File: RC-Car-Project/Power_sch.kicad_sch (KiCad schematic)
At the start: 0 parts

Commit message: Power: add converters
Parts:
- added C1, C2: 10u/50V, symbol Device:C
- added U2: XL1509-5.0, Package_SO:SOIC-8_3.9x4.9mm_P1.27mm, symbol Regulator_Switching:XL1509-5.0
- added U3: LT1963AxST-3.3, Package_TO_SOT_SMD:SOT-223-3_TabPin2, symbol Regulator_Linear:LT1963AxST-3.3
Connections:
- new net: C1.1, U3.1 (IN)
- new net: U2.5 (GND), U2.6 (GND), U2.7 (GND), U2.8 (GND)
- new net +3V3: C2.1, U3.3 (OUT)
- new net GND_3V3: C2.2, U3.2 (GND)
- new net GND_BATT: C1.2
- new net VDD_BATT: U2.1 (VIN)

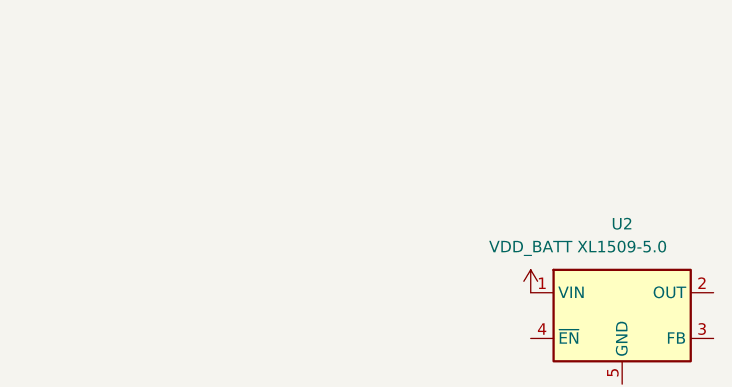
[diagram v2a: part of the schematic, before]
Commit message: Add libraries and components in schs
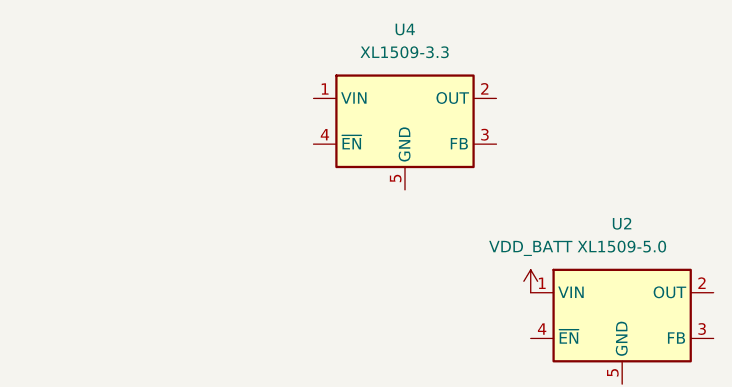
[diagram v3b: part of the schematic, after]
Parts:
- added U4: XL1509-3.3, Package_SO:SOIC-8_3.9x4.9mm_P1.27mm, symbol Regulator_Switching:XL1509-3.3
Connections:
- new net: U4.5 (GND), U4.6 (GND), U4.7 (GND), U4.8 (GND)
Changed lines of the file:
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@@
+	)
+	(symbol
+		(lib_id "Regulator_Switching:XL1509-3.3")
+		(at 143.51 48.26 0)
+		(unit 1)
+		(exclude_from_sim no)
+		(in_bom yes)
+		(on_board yes)
+		(dnp no)
+		(fields_autoplaced yes)
+		(property "Reference" "U4"
+			(at 143.51 38.1 0)
+			(effects
+				(font
+					(size 1.27 1.27)
+				)
+			)
+		)
+		(property "Value" "XL1509-3.3"
+			(at 143.51 40.64 0)
+			(effects
+				(font
+					(size 1.27 1.27)
+				)
+			)
+		)
+		(property "Footprint" "Package_SO:SOIC-8_3.9x4.9mm_P1.27mm"
+			(at 143.51 39.878 0)
+			(effects
+				(font
+					(size 1.27 1.27)
+				)
+				(hide yes)
+			)
+		)
+		(property "Datasheet" "https://datasheet.lcsc.com/lcsc/1809050422_XLSEMI-XL1509-5-0E1_C61063.pdf"
+			(at 146.05 37.592 0)
+			(effects
+				(font
+					(size 1.27 1.27)
+				)
+				(hide yes)
+			)
+		)
+		(property "Description" "Buck DC/DC Converter, 2A, 3.3V Output Voltage, 4.5-40V Input Voltage"
+			(at 143.51 48.26 0)
+			(effects
+				(font
+					(size 1.27 1.27)
+				)
+				(hide yes)
+			)
+		)
+		(pin "3"
+		)
+		(pin "2"
+		)
+		(pin "6"
+		)
+		(pin "7"
+		)
+		(pin "8"
+		)
+		(pin "5"
+		)
+		(pin "1"
+		)
+		(pin "4"
+		)
+		(instances
+			(project ""
+				(path "/ba870fd1-751d-4755-8e1a-1ea86ca9e2f6/e8cbdd69-5fc8-4583-a262-8a3c06e86dab"
+					(reference "U4")
+					(unit 1)
+				)
+			)
+		)
 	)
 	(symbol

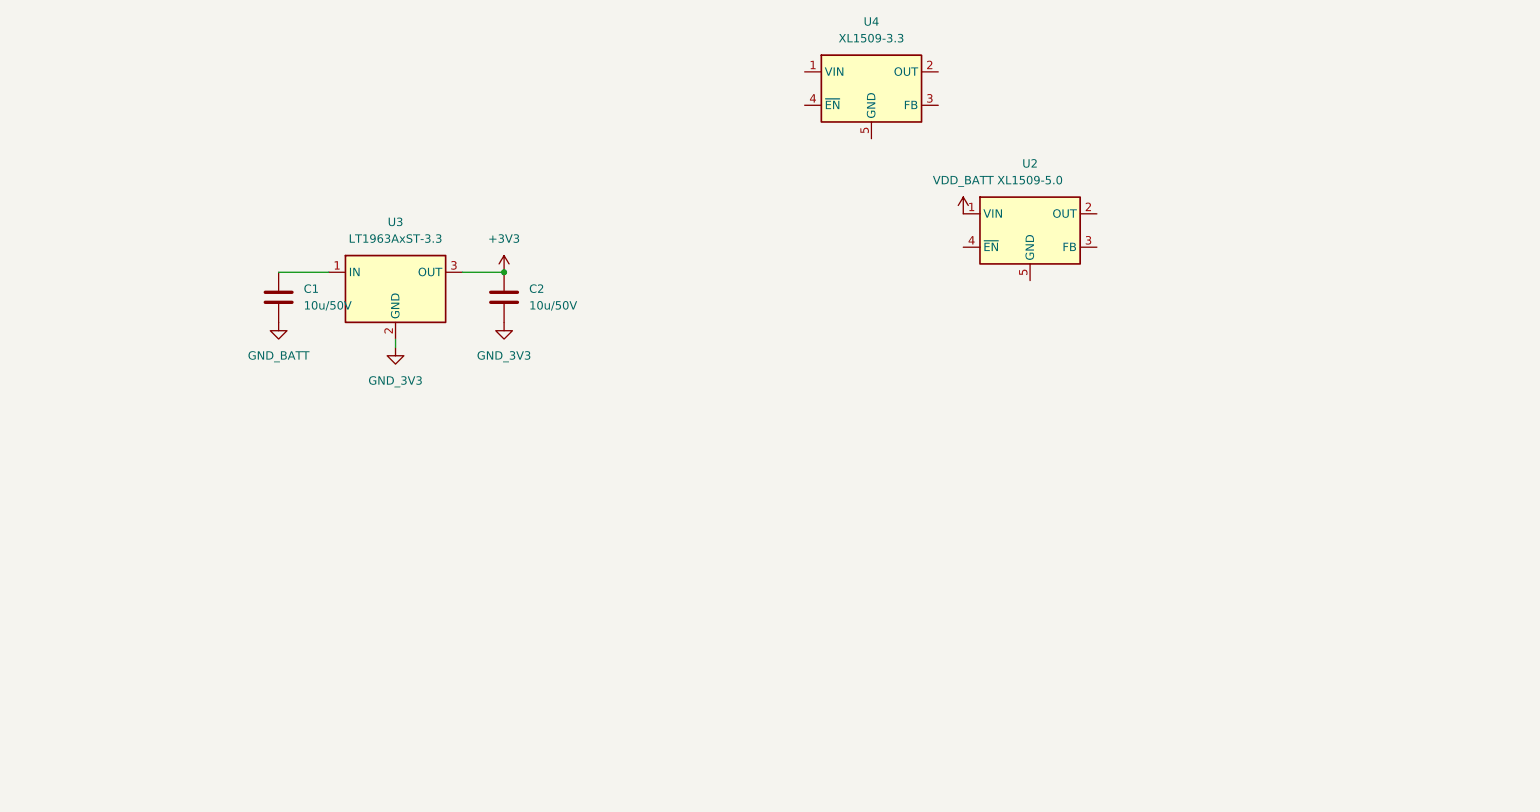
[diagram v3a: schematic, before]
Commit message: Added Basic Schematic + STM32 Project config. TODO: Component value selection + double check all connections.
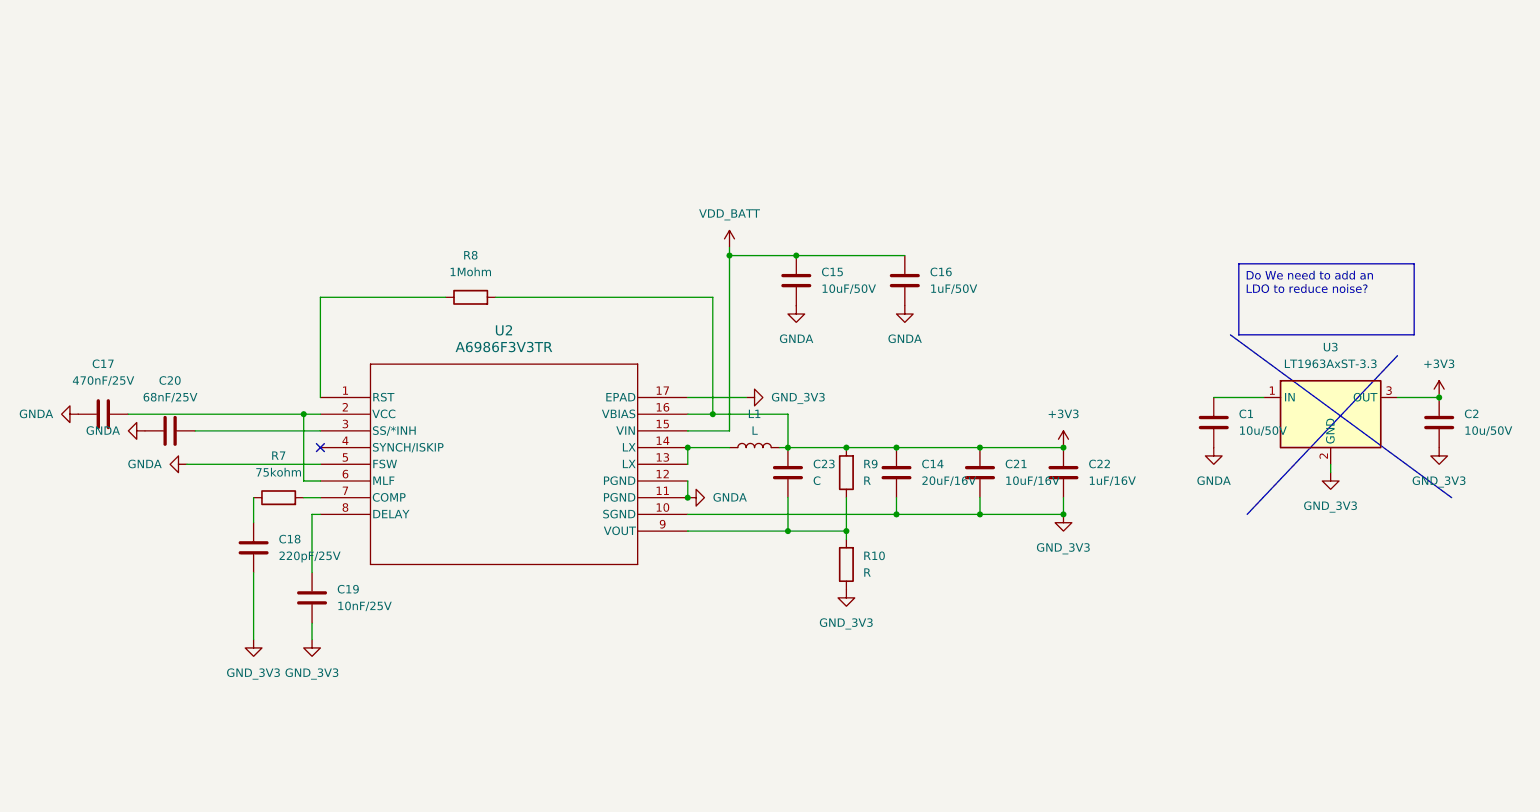
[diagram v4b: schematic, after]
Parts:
- removed U2: XL1509-5.0, Package_SO:SOIC-8_3.9x4.9mm_P1.27mm, symbol Regulator_Switching:XL1509-5.0
- removed U4: XL1509-3.3, Package_SO:SOIC-8_3.9x4.9mm_P1.27mm, symbol Regulator_Switching:XL1509-3.3
- added C14: 20uF/16V, symbol Device:C
- added C15: 10uF/50V, symbol Device:C
- added C16: 1uF/50V, symbol Device:C
- added C17: 470nF/25V, symbol Device:C
- added C18: 220pF/25V, symbol Device:C
- added C19: 10nF/25V, symbol Device:C
- added C20: 68nF/25V, symbol Device:C
- added C21: 10uF/16V, symbol Device:C
- added C22: 1uF/16V, symbol Device:C
- added C23: C, symbol Device:C
- added L1: L, symbol Device:L
- added R10, R9: R, symbol Device:R
- added R7: 75kohm, symbol Device:R
- added R8: 1Mohm, symbol Device:R
- added U2: A6986F3V3TR, HTSSOP16_4P5X5P1X0P65P_STM, symbol A6986F3V3TR:A6986F3V3TR
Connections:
- net +3V3: now also C14.1, C21.1, C22.1, C23.1, L1.2, R8.2, R9.2, U2.16 (VBIAS)
- net GND_3V3: now also C14.2, C18.1, C19.2, C21.2, C22.2, R10.1, U2.10 (SGND), U2.17 (EPAD)
- net VDD_BATT: now also C15.1, C16.1, U2.15 (VIN)
- net GND_BATT renamed GNDA
- net GNDA: now also C15.2, C16.2, C17.2, C20.2, U2.11 (PGND), U2.12 (PGND), U2.5 (FSW)
- new net: R8.1, U2.1 (RST)
- new net: L1.1, U2.13 (LX), U2.14 (LX)
- new net: C17.1, U2.2 (VCC), U2.6 (MLF)
- new net: C20.1, U2.3 (SS/*INH)
- new net: R7.2, U2.7 (COMP)
- new net: C19.1, U2.8 (DELAY)
- new net: C23.2, R10.2, R9.1, U2.9 (VOUT)
- new net: C18.2, R7.1
- no-connect marks 0 -> 1
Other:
- moved on the sheet: C1, C2, U3

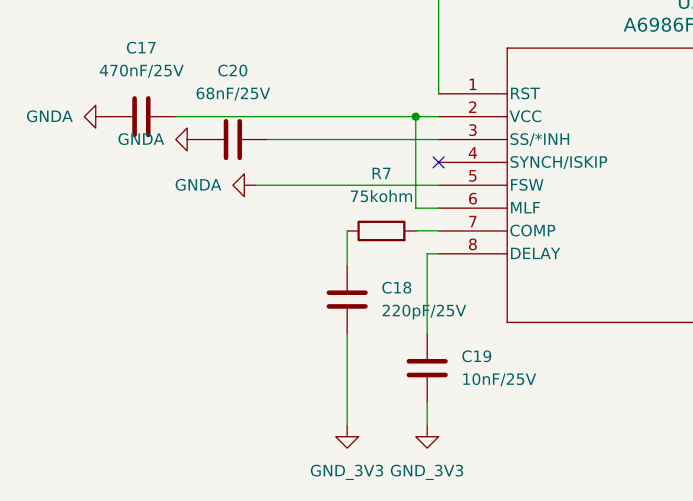
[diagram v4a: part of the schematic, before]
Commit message: Added footprints + final parts. (Need to finish buck converter next)
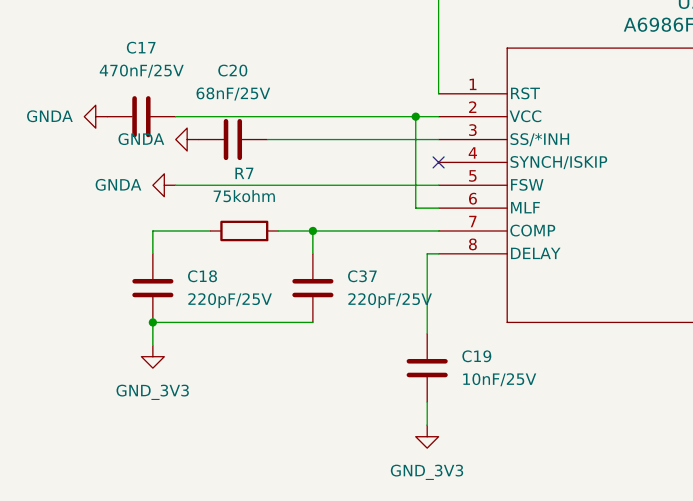
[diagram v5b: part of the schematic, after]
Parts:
- added C37: 220pF/25V, Capacitor_SMD:C_0201_0603Metric, symbol Device:C
- C16, C17, C18, C19, C20, C22, C23: footprint (none) -> Capacitor_SMD:C_0201_0603Metric
- L1: footprint (none) -> Inductor_SMD_Wurth:L_Wurth_WE-LQSH-4020
- R10, R7, R8, R9: footprint (none) -> Resistor_SMD:R_0201_0603Metric
- U2: footprint HTSSOP16_4P5X5P1X0P65P_STM -> footprints:HTSSOP16_4P5X5P1X0P65P_STM
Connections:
- net GND_3V3: now also C37.1
- net at R7.2, U2.7 (COMP): now also C37.2
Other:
- moved on the sheet: C18, R7
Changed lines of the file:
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@@
 	)
 	(junction
+		(at 27.94 120.65)
+		(diameter 0)
+		(color 0 0 0 0)
+	)
+	(junction
+		(at 45.72 110.49)
+		(diameter 0)
+		(color 0 0 0 0)
+	)
+	(junction
 		(at 130.81 115.57)
 		(diameter 0)
@@
 	(wire
 		(pts
+			(xy 45.72 113.03) (xy 45.72 110.49)
+		)
+		(stroke
+			(width 0)
+			(type default)
+		)
+	)
+	(wire
+		(pts
 			(xy 59.69 107.95) (xy 57.15 107.95)
 		)
@@
 	(wire
 		(pts
-			(xy 57.15 110.49) (xy 59.69 110.49)
+			(xy 41.91 110.49) (xy 45.72 110.49)
 		)
 		(stroke
@@
 	(wire
 		(pts
+			(xy 27.94 110.49) (xy 34.29 110.49)
+		)
+		(stroke
+			(width 0)
+			(type default)
+		)
+	)
+	(wire
+		(pts
 			(xy 57.15 97.79) (xy 59.69 97.79)
 		)
@@
 	(wire
 		(pts
+			(xy 27.94 120.65) (xy 45.72 120.65)
+		)
+		(stroke
+			(width 0)
+			(type default)
+		)
+	)
+	(wire
+		(pts
 			(xy 58.42 113.03) (xy 59.69 113.03)
 		)
@@
 	(wire
 		(pts
+			(xy 45.72 110.49) (xy 59.69 110.49)
+		)
+		(stroke
+			(width 0)
+			(type default)
+		)
+	)
+	(wire
+		(pts
 			(xy 130.81 102.87) (xy 139.7 102.87)
 		)
@@
 	(wire
 		(pts
-			(xy 59.69 80.01) (xy 78.74 80.01)
+			(xy 27.94 110.49) (xy 27.94 113.03)
 		)
 		(stroke
@@
 	(wire
 		(pts
-			(xy 115.57 102.87) (xy 121.92 102.87)
+			(xy 59.69 80.01) (xy 78.74 80.01)
 		)
 		(stroke
@@
 	(wire
 		(pts
-			(xy 121.92 73.66) (xy 121.92 100.33)
+			(xy 115.57 102.87) (xy 121.92 102.87)
 		)
 		(stroke
@@
 	(wire
 		(pts
-			(xy 119.38 80.01) (xy 119.38 97.79)
+			(xy 121.92 73.66) (xy 121.92 100.33)
 		)
 		(stroke
@@
 	(wire
 		(pts
-			(xy 130.81 102.87) (xy 130.81 97.79)
+			(xy 119.38 80.01) (xy 119.38 97.79)
 		)
 		(stroke
@@
 	(wire
 		(pts
-			(xy 58.42 121.92) (xy 58.42 113.03)
+			(xy 130.81 102.87) (xy 130.81 97.79)
 		)
 		(stroke
@@
 	(wire
 		(pts
-			(xy 49.53 110.49) (xy 49.53 114.3)
+			(xy 58.42 121.92) (xy 58.42 113.03)
 		)
 		(stroke
@@
 	(wire
 		(pts
-			(xy 39.37 105.41) (xy 59.69 105.41)
+			(xy 30.48 105.41) (xy 59.69 105.41)
 		)
 		(stroke
@@
 	(wire
 		(pts
-			(xy 49.53 132.08) (xy 49.53 121.92)
+			(xy 27.94 123.19) (xy 27.94 120.65)
 		)
 		(stroke
@@
 	(symbol
 		(lib_id "power:GND")
-		(at 49.53 132.08 0)
+		(at 27.94 123.19 0)
 		(unit 1)
 		(exclude_from_sim no)
@@
 		(fields_autoplaced yes)
 		(property "Reference" "#PWR045"
-			(at 49.53 138.43 0)
+			(at 27.94 129.54 0)
 			(effects
 				(font
@@
 		)
 		(property "Value" "GND_3V3"
-			(at 49.53 137.16 0)
+			(at 27.94 128.27 0)
 			(effects
 				(font
@@
 		)
 		(property "Footprint" ""
-			(at 49.53 132.08 0)
+			(at 27.94 123.19 0)
 			(effects
 				(font
@@
 		)
 		(property "Datasheet" ""
-			(at 49.53 132.08 0)
+			(at 27.94 123.19 0)
 			(effects
 				(font
@@
 		)
 		(property "Description" "Power symbol creates a global label with name \"GND\" , ground"
-			(at 49.53 132.08 0)
+			(at 27.94 123.19 0)
 			(effects
 				(font
@@
 			)
 		)
-		(property "Footprint" "HTSSOP16_4P5X5P1X0P65P_STM"
+		(property "Footprint" "footprints:HTSSOP16_4P5X5P1X0P65P_STM"
 			(at 59.69 95.25 0)
 			(effects
@@
 			)
 		)
-		(property "Footprint" ""
+		(property "Footprint" "Capacitor_SMD:C_0201_0603Metric"
 			(at 22.86 98.7552 0)
 			(effects
@@
 			)
 		)
-		(property "Footprint" ""
+		(property "Footprint" "Inductor_SMD_Wurth:L_Wurth_WE-LQSH-4020"
 			(at 125.73 102.87 0)
 			(effects
@@
 	(symbol
 		(lib_id "Device:R")
-		(at 53.34 110.49 90)
+		(at 38.1 110.49 90)
 		(unit 1)
 		(exclude_from_sim no)
@@
 		(fields_autoplaced yes)
 		(property "Reference" "R7"
-			(at 53.34 104.14 90)
+			(at 38.1 104.14 90)
 			(effects
 				(font
@@
 		)
 		(property "Value" "75kohm"
-			(at 53.34 106.68 90)
+			(at 38.1 106.68 90)
 			(effects
 				(font
@@
 			)
 		)
-		(property "Footprint" ""
-			(at 53.34 112.268 90)
+		(property "Footprint" "Resistor_SMD:R_0201_0603Metric"
+			(at 38.1 112.268 90)
 			(effects
 				(font
@@
 		)
 		(property "Datasheet" "~"
-			(at 53.34 110.49 0)
+			(at 38.1 110.49 0)
 			(effects
 				(font
@@
 		)
 		(property "Description" "Resistor"
-			(at 53.34 110.49 0)
+			(at 38.1 110.49 0)
 			(effects
 				(font
@@
 			)
 		)
-		(property "Footprint" ""
+		(property "Footprint" "Capacitor_SMD:C_0201_0603Metric"
 			(at 33.02 101.2952 0)
 			(effects
@@
 			)
 		)
-		(property "Footprint" ""
+		(property "Footprint" "Capacitor_SMD:C_0201_0603Metric"
 			(at 173.6852 110.49 0)
 			(effects
@@
 			)
 		)
-		(property "Footprint" ""
+		(property "Footprint" "Resistor_SMD:R_0201_0603Metric"
 			(at 141.478 120.65 90)
 			(effects
@@
 			)
 		)
-		(property "Footprint" ""
+		(property "Footprint" "Resistor_SMD:R_0201_0603Metric"
 			(at 82.55 81.788 90)
 			(effects
@@
 			)
 		)
-		(property "Footprint" ""
+		(property "Footprint" "Capacitor_SMD:C_0201_0603Metric"
 			(at 149.5552 81.28 0)
 			(effects
@@
 	(symbol
 		(lib_id "Device:C")
+		(at 45.72 116.84 180)
+		(unit 1)
+		(exclude_from_sim no)
+		(in_bom yes)
+		(on_board yes)
+		(dnp no)
+		(fields_autoplaced yes)
+		(property "Reference" "C37"
+			(at 49.53 115.5699 0)
+			(effects
+				(font
+					(size 1.27 1.27)
+				)
+				(justify right)
+			)
+		)
+		(property "Value" "220pF/25V"
+			(at 49.53 118.1099 0)
+			(effects
+				(font
+					(size 1.27 1.27)
+				)
+				(justify right)
+			)
+		)
+		(property "Footprint" "Capacitor_SMD:C_0201_0603Metric"
+			(at 44.7548 113.03 0)
+			(effects
+				(font
+					(size 1.27 1.27)
+				)
+				(hide yes)
+			)
+		)
+		(property "Datasheet" "~"
+			(at 45.72 116.84 0)
+			(effects
+				(font
+					(size 1.27 1.27)
+				)
+				(hide yes)
+			)
+		)
+		(property "Description" "Unpolarized capacitor"
+			(at 45.72 116.84 0)
+			(effects
+				(font
+					(size 1.27 1.27)
+				)
+				(hide yes)
+			)
+		)
+		(pin "1"
+		)
+		(pin "2"
+		)
+		(instances
+			(project "RC-Car-Project"
+				(path "/ba870fd1-751d-4755-8e1a-1ea86ca9e2f6/e8cbdd69-5fc8-4583-a262-8a3c06e86dab"
+					(reference "C37")
+					(unit 1)
+				)
+			)
+		)
+	)
+	(symbol
+		(lib_id "Device:C")
 		(at 130.81 106.68 0)
 		(unit 1)
@@
 			)
 		)
-		(property "Footprint" ""
+		(property "Footprint" "Capacitor_SMD:C_0201_0603Metric"
 			(at 131.7752 110.49 0)
 			(effects
@@
 	(symbol
 		(lib_id "Device:C")
-		(at 49.53 118.11 180)
+		(at 27.94 116.84 180)
 		(unit 1)
 		(exclude_from_sim no)
@@
 		(fields_autoplaced yes)
 		(property "Reference" "C18"
-			(at 53.34 116.8399 0)
+			(at 31.75 115.5699 0)
 			(effects
 				(font
@@
 		)
 		(property "Value" "220pF/25V"
-			(at 53.34 119.3799 0)
+			(at 31.75 118.1099 0)
 			(effects
 				(font
@@
 			)
 		)
-		(property "Footprint" ""
-			(at 48.5648 114.3 0)
+		(property "Footprint" "Capacitor_SMD:C_0201_0603Metric"
+			(at 26.9748 113.03 0)
 			(effects
 				(font
@@
 		)
 		(property "Datasheet" "~"
-			(at 49.53 118.11 0)
+			(at 27.94 116.84 0)
 			(effects
 				(font
@@
 		)
 		(property "Description" "Unpolarized capacitor"
-			(at 49.53 118.11 0)
+			(at 27.94 116.84 0)
 			(effects
 				(font
@@
 			)
 		)
-		(property "Footprint" ""
+		(property "Footprint" "Resistor_SMD:R_0201_0603Metric"
 			(at 141.478 106.68 90)
 			(effects
@@
 			)
 		)
-		(property "Footprint" ""
+		(property "Footprint" "Capacitor_SMD:C_0201_0603Metric"
 			(at 59.3852 129.54 0)
 			(effects
@@
 	(symbol
 		(lib_id "power:GNDA")
-		(at 39.37 105.41 270)
+		(at 30.48 105.41 270)
 		(unit 1)
 		(exclude_from_sim no)
@@
 		(fields_autoplaced yes)
 		(property "Reference" "#PWR048"
-			(at 33.02 105.41 0)
+			(at 24.13 105.41 0)
 			(effects
 				(font
@@
 		)
 		(property "Value" "GNDA"
-			(at 35.56 105.4099 90)
+			(at 26.67 105.4099 90)
 			(effects
 				(font
@@
 		)
 		(property "Footprint" ""
-			(at 39.37 105.41 0)
+			(at 30.48 105.41 0)
 			(effects
 				(font
@@
 		)
 		(property "Datasheet" ""
-			(at 39.37 105.41 0)
+			(at 30.48 105.41 0)
 			(effects
 				(font
@@
 		)
 		(property "Description" "Power symbol creates a global label with name \"GNDA\" , analog ground"
-			(at 39.37 105.41 0)
+			(at 30.48 105.41 0)
 			(effects
 				(font

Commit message: Finished Buck
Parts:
- removed C21: 10uF/16V, symbol Device:C
- removed U3: LT1963AxST-3.3, Package_TO_SOT_SMD:SOT-223-3_TabPin2, symbol Regulator_Linear:LT1963AxST-3.3
- added R21: 1.8kohm, Resistor_SMD:R_0201_0603Metric, symbol Device:R
- added R22: 56kohm, Resistor_SMD:R_0201_0603Metric, symbol Device:R
- C1: value 10u/50V -> 1uF/50V; footprint (none) -> Capacitor_SMD:C_0201_0603Metric
- C14: value 20uF/16V -> 10uF/50V; footprint (none) -> Capacitor_SMD:C_1210_3225Metric
- C15: footprint (none) -> Capacitor_SMD:C_1210_3225Metric
- C2: value 10u/50V -> 10uF/50V; footprint (none) -> Capacitor_SMD:C_1210_3225Metric
- C23: value C -> 220pF/16V
- L1: value L -> 8.2uH; footprint Inductor_SMD_Wurth:L_Wurth_WE-LQSH-4020 -> Inductor_SMD:L_Wuerth_MAPI-4030
- R10: value R -> 100kohm
- R9: value R -> 280kohm
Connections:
- net GNDA: now also R21.1; no longer U2.5 (FSW)
- net VDD_BATT: now also C1.1
- net at C17.1, U2.2 (VCC), U2.6 (MLF): now also R22.2
- new net: R21.2, R22.1, U2.5 (FSW)
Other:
- moved on the sheet: C15, C16, C17, C18, C19, C20, C22, C23, C37, L1, R10, R7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
